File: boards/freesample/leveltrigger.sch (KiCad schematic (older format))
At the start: 21 parts, among them U10 PI6C59S6005, U9 HMC675LP3E

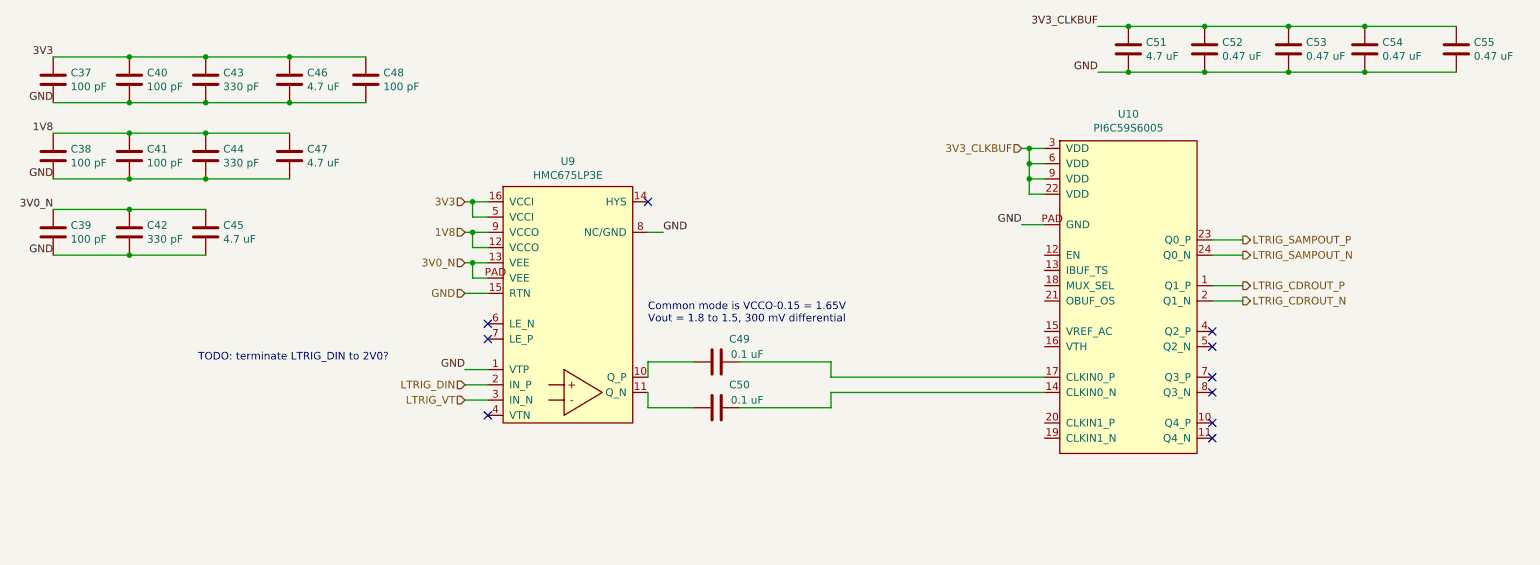
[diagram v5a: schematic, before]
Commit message: Continued schematic capture work. Hooked up most SoM connectors.
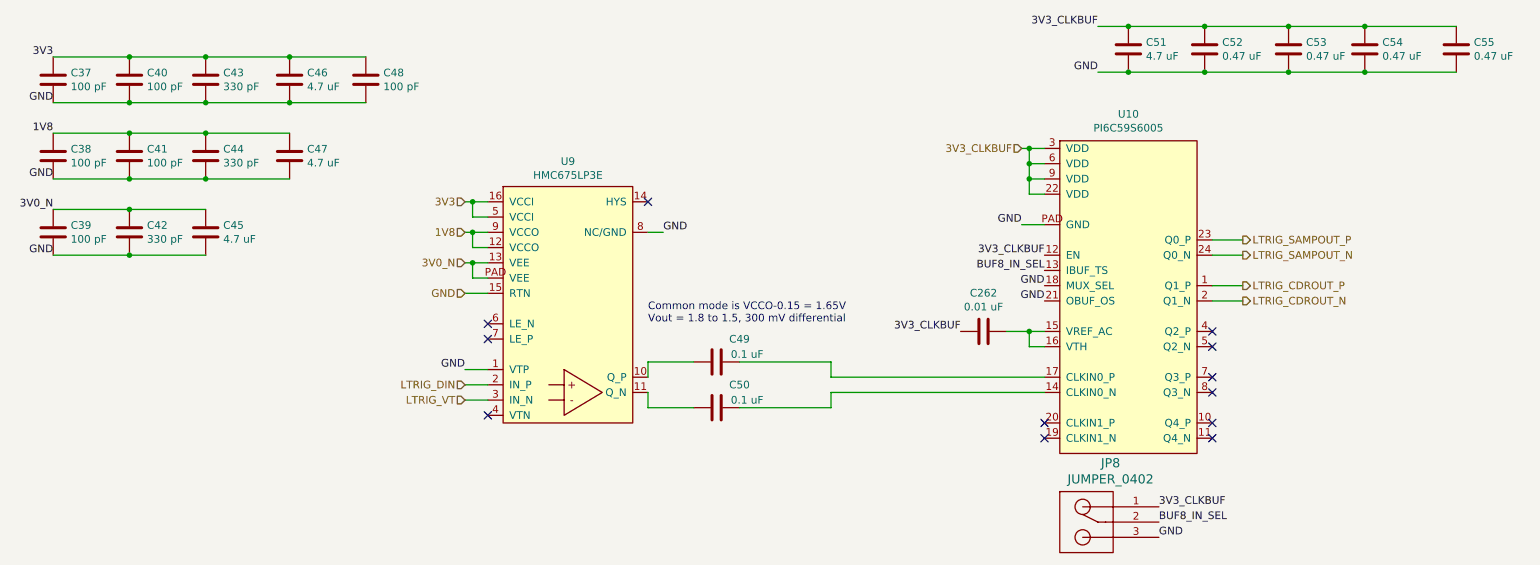
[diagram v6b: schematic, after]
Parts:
- added C262: 0.01 uF, symbol device:C
- added JP8: JUMPER_0402, symbol special-azonenberg:JUMPER_0402_SPDT
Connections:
- net 3V3_CLKBUF: now also U10.12 (EN), C262.2, JP8.1
- net GND: now also U10.18 (MUX_SEL), U10.21 (OBUF_OS), JP8.3
- net BUF8_IN_SEL: now reaches U10.13 (IBUF_TS)
- net BUF8_IN_SEL: now also JP8.2
- net at U10.15 (VREF_AC): now also U10.16 (VTH), C262.1
- no-connect marks 10 -> 12
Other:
- note removed: "TODO: terminate LTRIG_DIN to 2V0?"
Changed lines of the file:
@@
 Sheet 8 12
 Title "FREESAMPLE Oscilloscope"
-Date "2019-02-26"
+Date "2019-03-10"
 Rev "0.1"
 Comp "Andrew D. Zonenberg / Antikernel Labs"
 Comment1 "Level triggering"
-Comment2 ""
+Comment2 "Ready for review"
 Comment3 ""
 Comment4 ""
@@
 Wire Wire Line
 	8650 2450 8850 2450
-Text Notes 2000 2850 0    50   ~ 0
-TODO: terminate LTRIG_DIN to 2V0?
 Text Notes 4950 2600 0    50   ~ 0
 Common mode is VCCO-0.15 = 1.65V\nVout = 1.8 to 1.5, 300 mV differential
 Text HLabel 7400 1450 0    50   Input ~ 0
 3V3_CLKBUF
+Text Label 7550 2150 2    50   ~ 0
+3V3_CLKBUF
+NoConn ~ 7550 3250
+NoConn ~ 7550 3350
+Text Label 7550 2350 2    50   ~ 0
+GND
+Text Label 7550 2450 2    50   ~ 0
+GND
+Wire Wire Line
+	7550 2650 7450 2650
+Wire Wire Line
+	7450 2650 7450 2750
+Wire Wire Line
+	7450 2750 7550 2750
+$Comp
+L device:C C262
+U 1 1 5D47E4DD
+P 7150 2650
+F 0 "C262" V 6898 2650 50  0000 C CNN
+F 1 "0.01 uF" V 6989 2650 50  0000 C CNN
+F 2 "" H 7188 2500 50  0001 C CNN
+F 3 "" H 7150 2650 50  0001 C CNN
+	1    7150 2650
+	0    1    1    0
+$EndComp
+Wire Wire Line
+	7300 2650 7450 2650
+Connection ~ 7450 2650
+Text Label 7000 2650 2    50   ~ 0
+3V3_CLKBUF
+$Comp
+L special-azonenberg:JUMPER_0402_SPDT JP?
+U 1 1 5D486796
+P 8000 4100
+AR Path="/5C0E404A/5D486796" Ref="JP?"  Part="1"
+AR Path="/5C23AE1C/5D486796" Ref="JP8"  Part="1"
+F 0 "JP8" H 7983 4687 60  0000 C CNN
+F 1 "JUMPER_0402" H 7983 4581 60  0000 C CNN
+F 2 "" H 8000 4100 60  0000 C CNN
+F 3 "" H 8000 4100 60  0000 C CNN
+	1    8000 4100
+	1    0    0    -1
+$EndComp
+Text Label 8300 3900 0    50   ~ 0
+BUF8_IN_SEL
+Text Label 8300 3800 0    50   ~ 0
+3V3_CLKBUF
+Text Label 8300 4000 0    50   ~ 0
+GND
+Text Label 7550 2250 2    50   ~ 0
+BUF8_IN_SEL
 $EndSCHEMATC

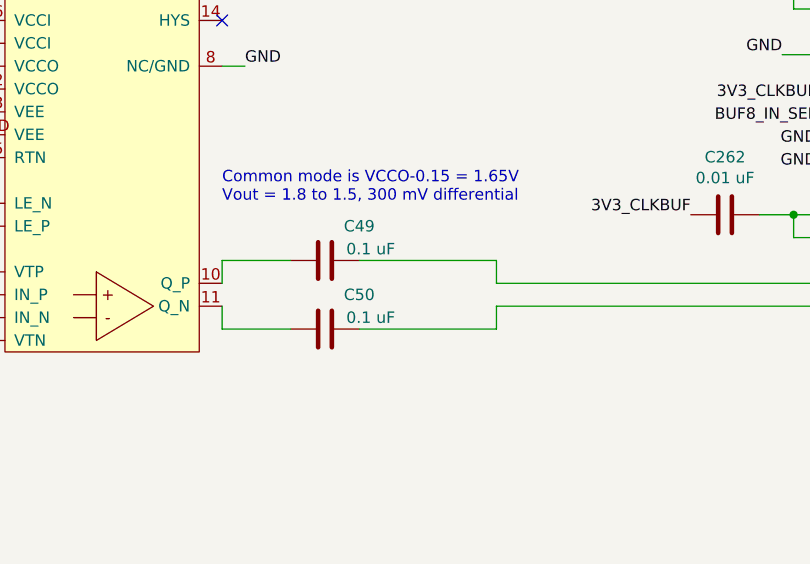
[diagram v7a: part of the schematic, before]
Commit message: Specified part number for AC coupling caps
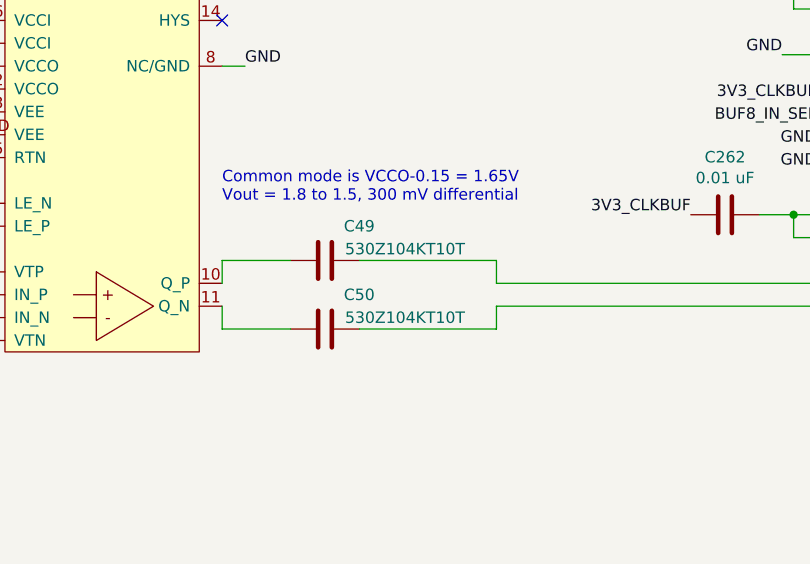
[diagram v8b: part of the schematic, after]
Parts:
- C49, C50: value 0.1 uF -> 530Z104KT10T
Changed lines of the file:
@@
 Sheet 8 12
 Title "FREESAMPLE Oscilloscope"
-Date "2019-03-11"
+Date "2019-03-13"
 Rev "0.1"
 Comp "Andrew D. Zonenberg / Antikernel Labs"
@@
 P 5400 2850
 F 0 "C49" V 5250 3000 50  0000 C CNN
-F 1 "0.1 uF" V 5350 3050 50  0000 C CNN
+F 1 "530Z104KT10T" V 5350 3200 50  0000 C CNN
 F 2 "" H 5438 2700 50  0001 C CNN
 F 3 "" H 5400 2850 50  0001 C CNN
@@
 P 5400 3150
 F 0 "C50" V 5250 3300 50  0000 C CNN
-F 1 "0.1 uF" V 5350 3350 50  0000 C CNN
+F 1 "530Z104KT10T" V 5350 3500 50  0000 C CNN
 F 2 "" H 5438 3000 50  0001 C CNN
 F 3 "" H 5400 3150 50  0001 C CNN
